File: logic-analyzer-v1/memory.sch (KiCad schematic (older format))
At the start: 8 parts

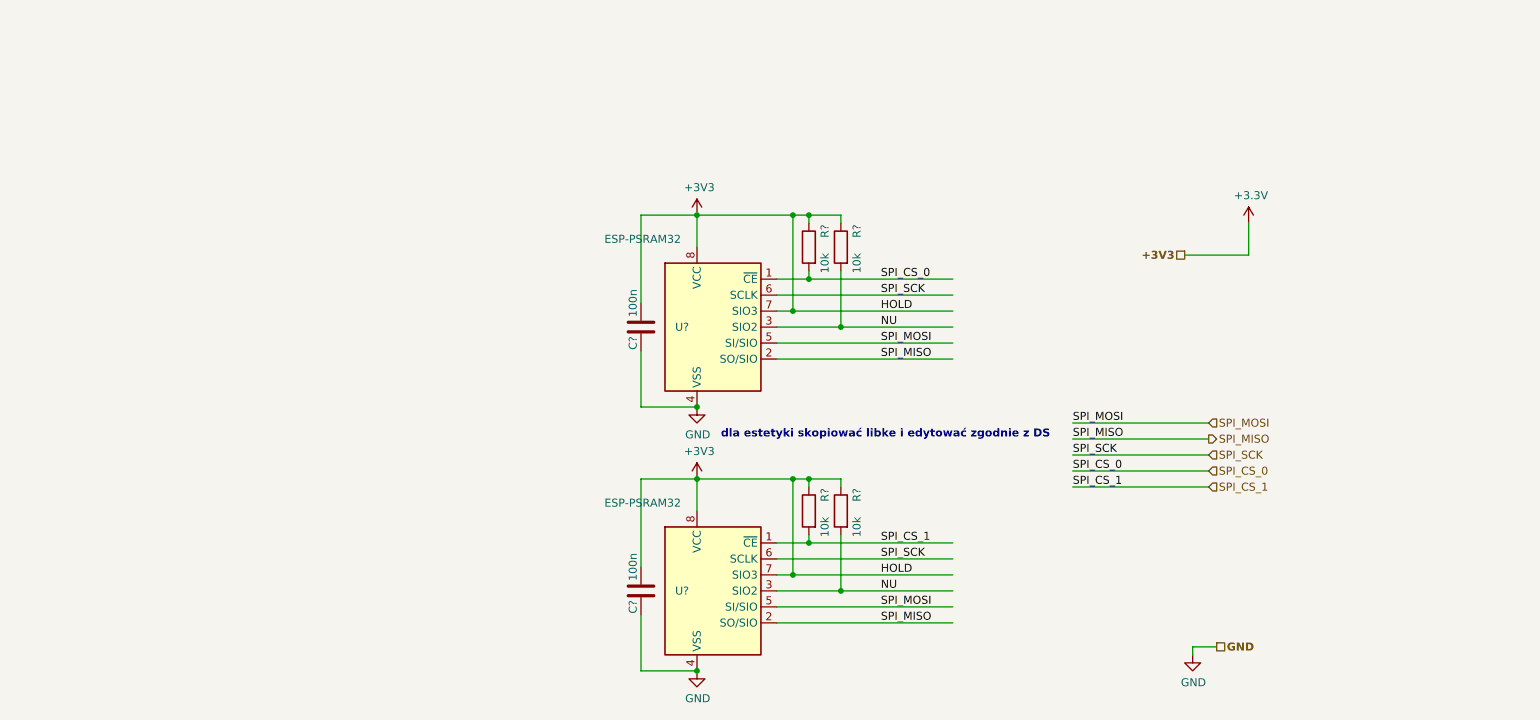
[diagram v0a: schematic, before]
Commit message: add comparator&sram
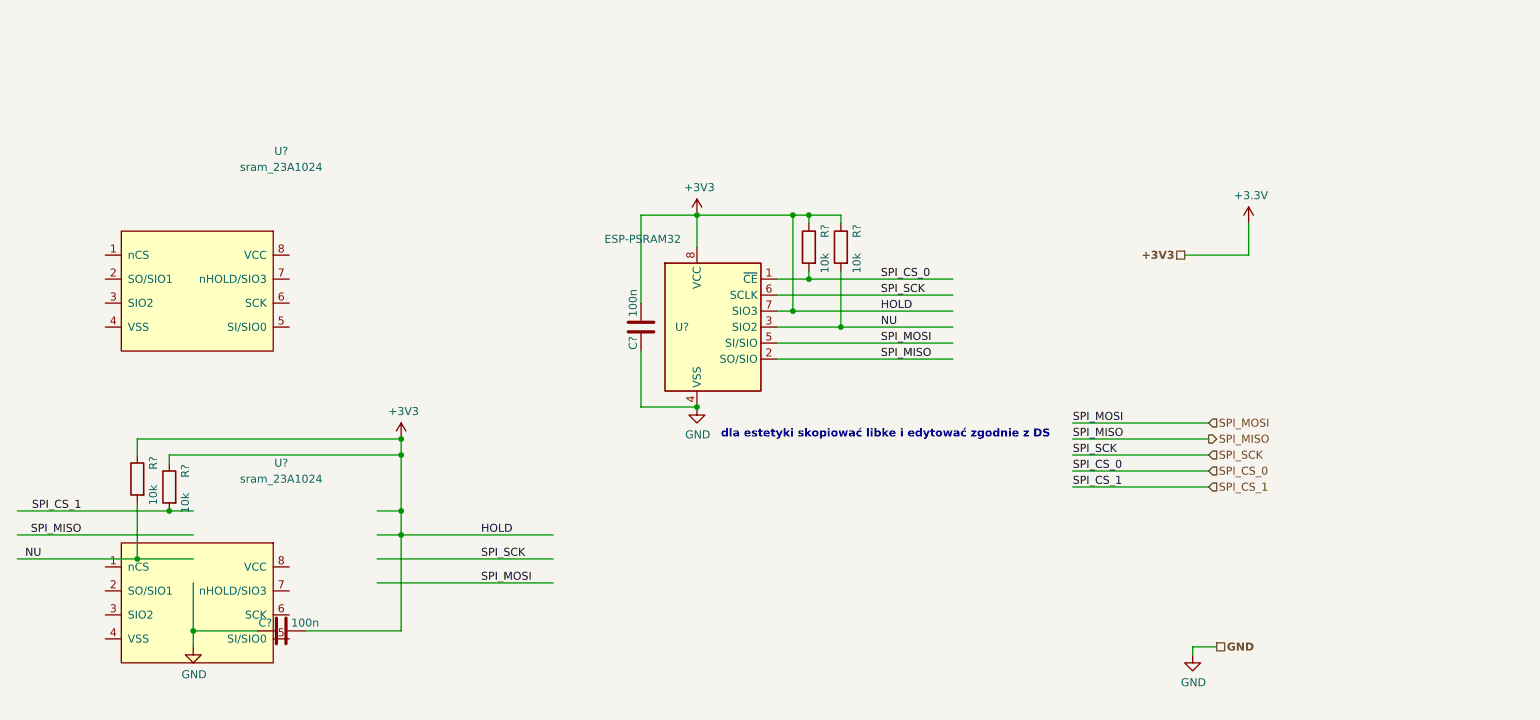
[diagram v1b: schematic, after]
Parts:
- removed C?: 100n, Capacitor_SMD:C_0603_1608Metric_Pad1.05x0.95mm_HandSolder, symbol Device:C
- removed U?: ESP-PSRAM32, Package_SO:SOIC-8_3.9x4.9mm_P1.27mm, symbol Memory_RAM:ESP-PSRAM32
- added C?: 100n, Capacitor_SMD:C_0603_1608Metric_Pad1.05x0.95mm_HandSolder, symbol Device:C
- added U? (x2): sram_23A1024, symbol New_Library:sram_23A1024
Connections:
- wire segments 53 -> 54
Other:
- moved on the sheet: R?
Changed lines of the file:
@@
 F 1 "ESP-PSRAM32" H 4800 3700 50  0000 R CNN
 F 2 "Package_SO:SOIC-8_3.9x4.9mm_P1.27mm" H 5000 2550 50  0001 C CNN
-F 3 "https://www.espressif.com/sites/default/files/documentation/esp-psram32_datasheet_en.pdf" H 4600 3650 50  0001 C CNN
+F 3 "https://www.tme.eu/Document/745fc52173836ec906dd19c8a3a18eb9/20005142C.pdf" H 4600 3650 50  0001 C CNN
 	1    5000 3150
 	1    0    0    -1
@@
 	4900 2450 4550 2450
 Connection ~ 4900 3650
-$Comp
-L Memory_RAM:ESP-PSRAM32 U?
-U 1 1 5FDC3CEF
-P 5000 4800
-AR Path="/5F19654C/5FDC3CEF" Ref="U?"  Part="1"
-AR Path="/5FDBE2FD/5FDC3CEF" Ref="U?"  Part="1"
-F 0 "U?" H 4850 4800 50  0000 R CNN
-F 1 "ESP-PSRAM32" H 4800 5350 50  0000 R CNN
-F 2 "Package_SO:SOIC-8_3.9x4.9mm_P1.27mm" H 5000 4200 50  0001 C CNN
-F 3 "https://www.espressif.com/sites/default/files/documentation/esp-psram32_datasheet_en.pdf" H 4600 5300 50  0001 C CNN
-	1    5000 4800
-	1    0    0    -1
-$EndComp
-$Comp
-L power:+3V3 #PWR?
-U 1 1 5FDC3CF5
-P 4900 4100
-AR Path="/5F19654C/5FDC3CF5" Ref="#PWR?"  Part="1"
-AR Path="/5FDBE2FD/5FDC3CF5" Ref="#PWR?"  Part="1"
-F 0 "#PWR?" H 4900 3950 50  0001 C CNN
-F 1 "+3V3" H 4915 4273 50  0000 C CNN
-F 2 "" H 4900 4100 50  0001 C CNN
-F 3 "" H 4900 4100 50  0001 C CNN
-	1    4900 4100
-	1    0    0    -1
-$EndComp
-$Comp
-L power:GND #PWR?
-U 1 1 5FDC3CFB
-P 4900 5300
-AR Path="/5F19654C/5FDC3CFB" Ref="#PWR?"  Part="1"
-AR Path="/5FDBE2FD/5FDC3CFB" Ref="#PWR?"  Part="1"
-F 0 "#PWR?" H 4900 5050 50  0001 C CNN
-F 1 "GND" H 4905 5127 50  0000 C CNN
-F 2 "" H 4900 5300 50  0001 C CNN
-F 3 "" H 4900 5300 50  0001 C CNN
-	1    4900 5300
-	1    0    0    -1
-$EndComp
-$Comp
-L Device:C C?
-U 1 1 5FDC3D17
-P 4550 4800
-AR Path="/5F19654C/5FDC3D17" Ref="C?"  Part="1"
-AR Path="/5FDBE2FD/5FDC3D17" Ref="C?"  Part="1"
-F 0 "C?" V 4500 4700 50  0000 C CNN
-F 1 "100n" V 4500 4950 50  0000 C CNN
-F 2 "Capacitor_SMD:C_0603_1608Metric_Pad1.05x0.95mm_HandSolder" H 4588 4650 50  0001 C CNN
-F 3 "~" H 4550 4800 50  0001 C CNN
-	1    4550 4800
-	1    0    0    -1
-$EndComp
-Wire Wire Line
-	4900 5300 4550 5300
-Wire Wire Line
-	4550 5300 4550 4950
-Wire Wire Line
-	4900 4100 4550 4100
-Connection ~ 4900 5300
 Text Notes 5050 3850 0    50   ~ 10
 dla estetyki skopiować libke i edytować zgodnie z DS
@@
 Wire Wire Line
 	5600 2850 6500 2850
-Text Label 6050 4900 0    50   ~ 0
-SPI_MOSI
-Text Label 6050 5000 0    50   ~ 0
+Text Label 1050 4450 2    50   ~ 0
 SPI_MISO
-Text Label 6050 4600 0    50   ~ 0
+Text Label 3550 4600 0    50   ~ 0
 SPI_SCK
-Text Label 6050 4500 0    50   ~ 0
+Text Label 1050 4300 2    50   ~ 0
 SPI_CS_1
-Text Label 6050 4700 0    50   ~ 0
-HOLD
 $Comp
 L Device:R R?
 U 1 1 5FDDAAEC
-P 5800 4300
+P 1400 4100
 AR Path="/5F08ED8D/5FDDAAEC" Ref="R?"  Part="1"
 AR Path="/5F19654C/5FDDAAEC" Ref="R?"  Part="1"
 AR Path="/5FDBE2FD/5FDDAAEC" Ref="R?"  Part="1"
-F 0 "R?" V 5700 4400 50  0000 C CNN
-F 1 "10k" V 5700 4200 50  0000 C CNN
-F 2 "Resistor_SMD:R_0603_1608Metric_Pad1.05x0.95mm_HandSolder" V 5730 4300 50  0001 C CNN
-F 3 "~" H 5800 4300 50  0001 C CNN
-	1    5800 4300
+F 0 "R?" V 1300 4200 50  0000 C CNN
+F 1 "10k" V 1300 4000 50  0000 C CNN
+F 2 "Resistor_SMD:R_0603_1608Metric_Pad1.05x0.95mm_HandSolder" V 1330 4100 50  0001 C CNN
+F 3 "~" H 1400 4100 50  0001 C CNN
+	1    1400 4100
 	-1   0    0    -1
 $EndComp
@@
 L Device:R R?
 U 1 1 5FDDAAF2
-P 5600 4300
+P 1600 4150
 AR Path="/5F08ED8D/5FDDAAF2" Ref="R?"  Part="1"
 AR Path="/5F19654C/5FDDAAF2" Ref="R?"  Part="1"
 AR Path="/5FDBE2FD/5FDDAAF2" Ref="R?"  Part="1"
-F 0 "R?" V 5500 4400 50  0000 C CNN
-F 1 "10k" V 5500 4200 50  0000 C CNN
-F 2 "Resistor_SMD:R_0603_1608Metric_Pad1.05x0.95mm_HandSolder" V 5530 4300 50  0001 C CNN
-F 3 "~" H 5600 4300 50  0001 C CNN
-	1    5600 4300
+F 0 "R?" V 1500 4250 50  0000 C CNN
+F 1 "10k" V 1500 4050 50  0000 C CNN
+F 2 "Resistor_SMD:R_0603_1608Metric_Pad1.05x0.95mm_HandSolder" V 1530 4150 50  0001 C CNN
+F 3 "~" H 1600 4150 50  0001 C CNN
+	1    1600 4150
 	-1   0    0    -1
 $EndComp
-Text Label 6050 4800 0    50   ~ 0
+Text Label 800  4600 2    50   ~ 0
 NU
 Wire Wire Line
-	5600 4150 5600 4100
-Connection ~ 5600 4100
-Wire Wire Line
-	5600 4100 5800 4100
-Wire Wire Line
-	5800 4100 5800 4150
-Wire Wire Line
-	4900 4100 5500 4100
-Wire Wire Line
-	5500 4700 5500 4100
-Connection ~ 5500 4100
-Wire Wire Line
-	5500 4100 5600 4100
-Wire Wire Line
-	5500 4700 5400 4700
-Connection ~ 5500 4700
-Wire Wire Line
-	5400 4900 6500 4900
-Wire Wire Line
-	5400 5000 6500 5000
-Wire Wire Line
-	5400 4800 5800 4800
-Wire Wire Line
-	5500 4700 6500 4700
-Wire Wire Line
-	5400 4600 6500 4600
-Wire Wire Line
-	5400 4500 5600 4500
-Wire Wire Line
-	5800 4450 5800 4800
-Connection ~ 5800 4800
-Wire Wire Line
-	5800 4800 6500 4800
-Wire Wire Line
-	5600 4450 5600 4500
-Connection ~ 5600 4500
-Wire Wire Line
-	5600 4500 6500 4500
-Connection ~ 4900 4100
-Wire Wire Line
-	4550 4100 4550 4650
-Wire Wire Line
-	4900 4300 4900 4100
+	1750 4450 650  4450
+Wire Wire Line
+	2900 4600 4000 4600
+Wire Wire Line
+	1750 4600 1400 4600
+Wire Wire Line
+	1750 4300 1600 4300
 Text HLabel 8100 3750 2    50   Input ~ 0
 SPI_MOSI
@@
 Wire Wire Line
 	8350 2700 8350 2500
+$Comp
+L New_Library:sram_23A1024 U?
+U 1 1 6063BECA
+P 1750 2900
+F 0 "U?" H 2300 3750 50  0000 C CNN
+F 1 "sram_23A1024" H 2300 3650 50  0000 C CNN
+F 2 "" H 2300 3600 50  0001 C CNN
+F 3 "https://www.tme.eu/pl/details/23lc1024-i_sn/pamieci-sram-szeregowe/microchip-technology/" H 2300 3600 50  0001 C CNN
+	1    1750 2900
+	1    0    0    -1
+$EndComp
+$Comp
+L New_Library:sram_23A1024 U?
+U 1 1 6064CBA0
+P 1750 4850
+F 0 "U?" H 2300 5700 50  0000 C CNN
+F 1 "sram_23A1024" H 2300 5600 50  0000 C CNN
+F 2 "" H 2300 5550 50  0001 C CNN
+F 3 "https://www.tme.eu/pl/details/23lc1024-i_sn/pamieci-sram-szeregowe/microchip-technology/" H 2300 5550 50  0001 C CNN
+	1    1750 4850
+	1    0    0    -1
+$EndComp
+$Comp
+L Device:C C?
+U 1 1 6064CE71
+P 2300 5050
+AR Path="/5F19654C/6064CE71" Ref="C?"  Part="1"
+AR Path="/5FDBE2FD/6064CE71" Ref="C?"  Part="1"
+F 0 "C?" V 2250 4950 50  0000 C CNN
+F 1 "100n" V 2250 5200 50  0000 C CNN
+F 2 "Capacitor_SMD:C_0603_1608Metric_Pad1.05x0.95mm_HandSolder" H 2338 4900 50  0001 C CNN
+F 3 "~" H 2300 5050 50  0001 C CNN
+	1    2300 5050
+	0    1    1    0
+$EndComp
+Wire Wire Line
+	2900 4300 3050 4300
+Wire Wire Line
+	3050 4300 3050 4450
+Wire Wire Line
+	3050 5050 2450 5050
+Wire Wire Line
+	1750 4750 1750 5050
+Wire Wire Line
+	1750 5050 2150 5050
+Wire Wire Line
+	3050 4300 3050 3950
+Connection ~ 3050 4300
+$Comp
+L power:GND #PWR?
+U 1 1 6065064B
+P 1750 5150
+AR Path="/5F19654C/6065064B" Ref="#PWR?"  Part="1"
+AR Path="/5FDBE2FD/6065064B" Ref="#PWR?"  Part="1"
+F 0 "#PWR?" H 1750 4900 50  0001 C CNN
+F 1 "GND" H 1755 4977 50  0000 C CNN
+F 2 "" H 1750 5150 50  0001 C CNN
+F 3 "" H 1750 5150 50  0001 C CNN
+	1    1750 5150
+	1    0    0    -1
+$EndComp
+$Comp
+L power:+3V3 #PWR?
+U 1 1 60650961
+P 3050 3850
+AR Path="/5F19654C/60650961" Ref="#PWR?"  Part="1"
+AR Path="/5FDBE2FD/60650961" Ref="#PWR?"  Part="1"
+F 0 "#PWR?" H 3050 3700 50  0001 C CNN
+F 1 "+3V3" H 3065 4023 50  0000 C CNN
+F 2 "" H 3050 3850 50  0001 C CNN
+F 3 "" H 3050 3850 50  0001 C CNN
+	1    3050 3850
+	1    0    0    -1
+$EndComp
+Text Label 3550 4450 0    50   ~ 0
+HOLD
+Wire Wire Line
+	2900 4750 4000 4750
+Text Label 3550 4750 0    50   ~ 0
+SPI_MOSI
+Wire Wire Line
+	2900 4450 3050 4450
+Connection ~ 3050 4450
+Wire Wire Line
+	3050 4450 3050 5050
+Wire Wire Line
+	3050 4450 4000 4450
+Connection ~ 1600 4300
+Wire Wire Line
+	1600 4300 650  4300
+Wire Wire Line
+	1600 4000 1600 3950
+Wire Wire Line
+	1600 3950 3050 3950
+Connection ~ 3050 3950
+Wire Wire Line
+	3050 3950 3050 3850
+Wire Wire Line
+	3050 3850 1400 3850
+Connection ~ 3050 3850
+Wire Wire Line
+	1400 3850 1400 3950
+Wire Wire Line
+	1400 4250 1400 4600
+Connection ~ 1400 4600
+Wire Wire Line
+	1400 4600 650  4600
+Connection ~ 1750 5050
+Wire Wire Line
+	1750 5050 1750 5150
 $EndSCHEMATC

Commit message: MOD uart port direction, minor cosmetic changes
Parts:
- U? (x2): symbol New_Library:sram_23A1024 -> logic-analyzer-v1-rescue:sram_23A1024-New_Library
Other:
- moved on the sheet: U?
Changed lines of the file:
@@
 $Descr A4 11693 8268
 encoding utf-8
-Sheet 5 6
+Sheet 5 8
 Title ""
 Date ""
@@
 	8350 2700 8350 2500
 $Comp
-L New_Library:sram_23A1024 U?
+L logic-analyzer-v1-rescue:sram_23A1024-New_Library U?
 U 1 1 6063BECA
 P 1750 2900
@@
 $EndComp
 $Comp
-L New_Library:sram_23A1024 U?
+L logic-analyzer-v1-rescue:sram_23A1024-New_Library U?
 U 1 1 6064CBA0
 P 1750 4850

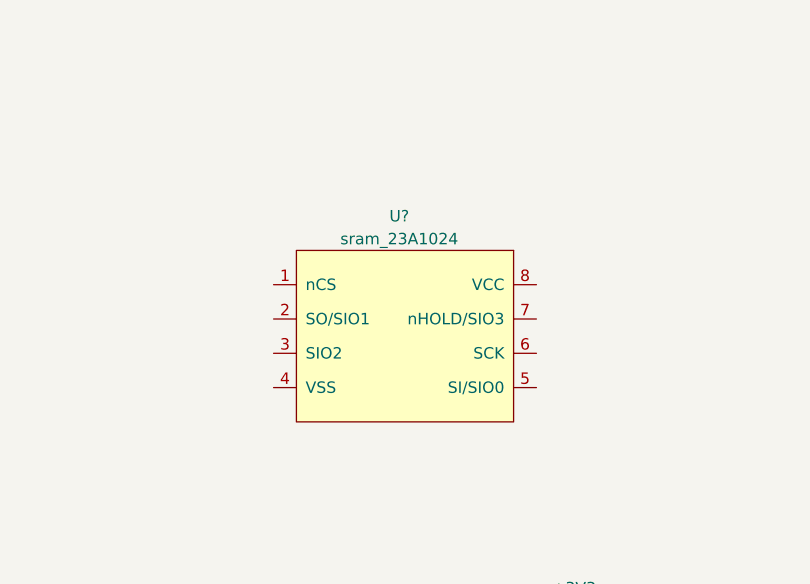
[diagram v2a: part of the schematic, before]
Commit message: improvement origin in libraries and creation my_library containing all ours libraries
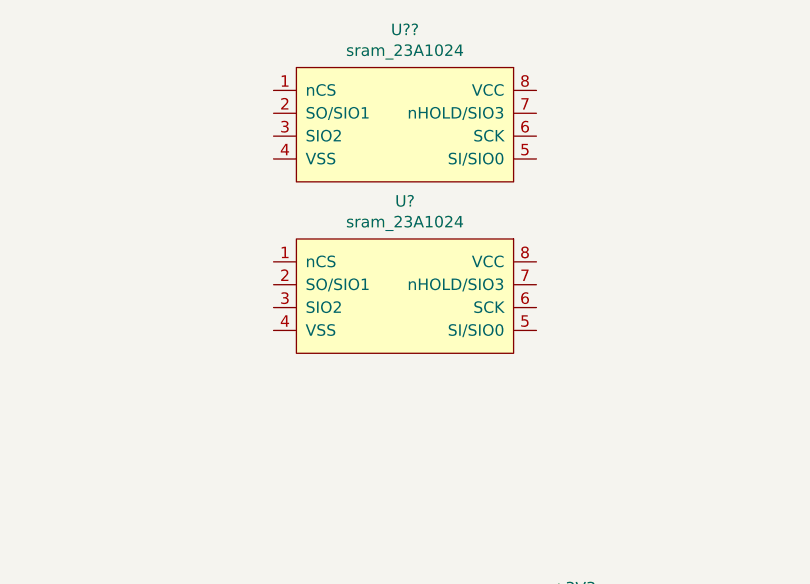
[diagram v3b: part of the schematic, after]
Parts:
- removed U?: sram_23A1024, symbol logic-analyzer-v1-rescue:sram_23A1024-New_Library
- added U?, U??: sram_23A1024, symbol my_library:sram_23A1024
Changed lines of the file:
@@
 $Descr A4 11693 8268
 encoding utf-8
-Sheet 5 8
+Sheet 7 8
 Title ""
 Date ""
@@
 $Comp
 L logic-analyzer-v1-rescue:sram_23A1024-New_Library U?
-U 1 1 6063BECA
-P 1750 2900
-F 0 "U?" H 2300 3750 50  0000 C CNN
-F 1 "sram_23A1024" H 2300 3650 50  0000 C CNN
-F 2 "" H 2300 3600 50  0001 C CNN
-F 3 "https://www.tme.eu/pl/details/23lc1024-i_sn/pamieci-sram-szeregowe/microchip-technology/" H 2300 3600 50  0001 C CNN
-	1    1750 2900
-	1    0    0    -1
-$EndComp
-$Comp
-L logic-analyzer-v1-rescue:sram_23A1024-New_Library U?
 U 1 1 6064CBA0
 P 1750 4850
@@
 Wire Wire Line
 	1750 5050 1750 5150
+$Comp
+L my_library:sram_23A1024 U??
+U 1 1 60877B38
+P 2300 1650
+F 0 "U??" H 2325 2065 50  0000 C CNN
+F 1 "sram_23A1024" H 2325 1974 50  0000 C CNN
+F 2 "" H 2300 2000 50  0001 C CNN
+F 3 "" H 2300 2000 50  0001 C CNN
+	1    2300 1650
+	1    0    0    -1
+$EndComp
+$Comp
+L my_library:sram_23A1024 U?
+U 1 1 60878112
+P 2300 2400
+F 0 "U?" H 2325 2815 50  0000 C CNN
+F 1 "sram_23A1024" H 2325 2724 50  0000 C CNN
+F 2 "" H 2300 2750 50  0001 C CNN
+F 3 "" H 2300 2750 50  0001 C CNN
+	1    2300 2400
+	1    0    0    -1
+$EndComp
 $EndSCHEMATC

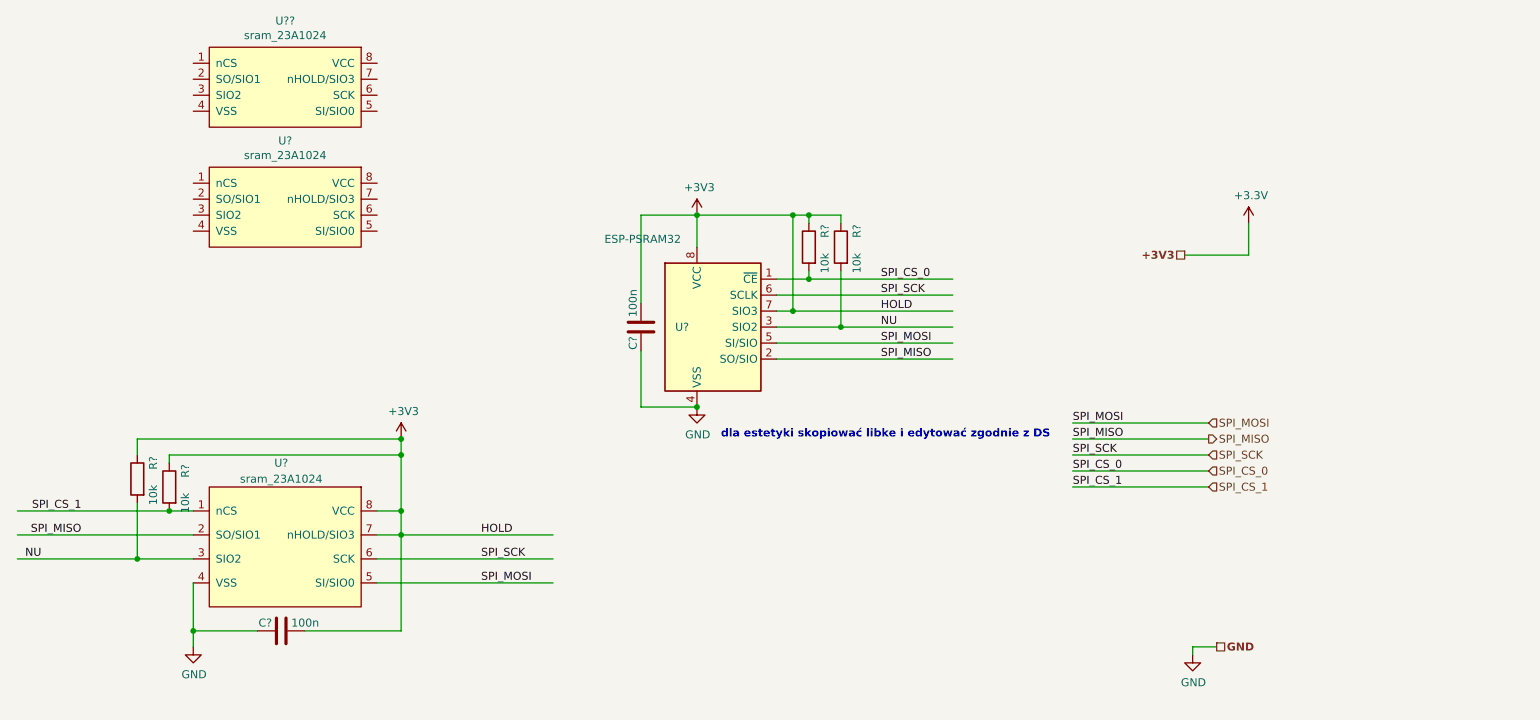
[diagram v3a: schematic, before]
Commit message: changing sram blocks from new library
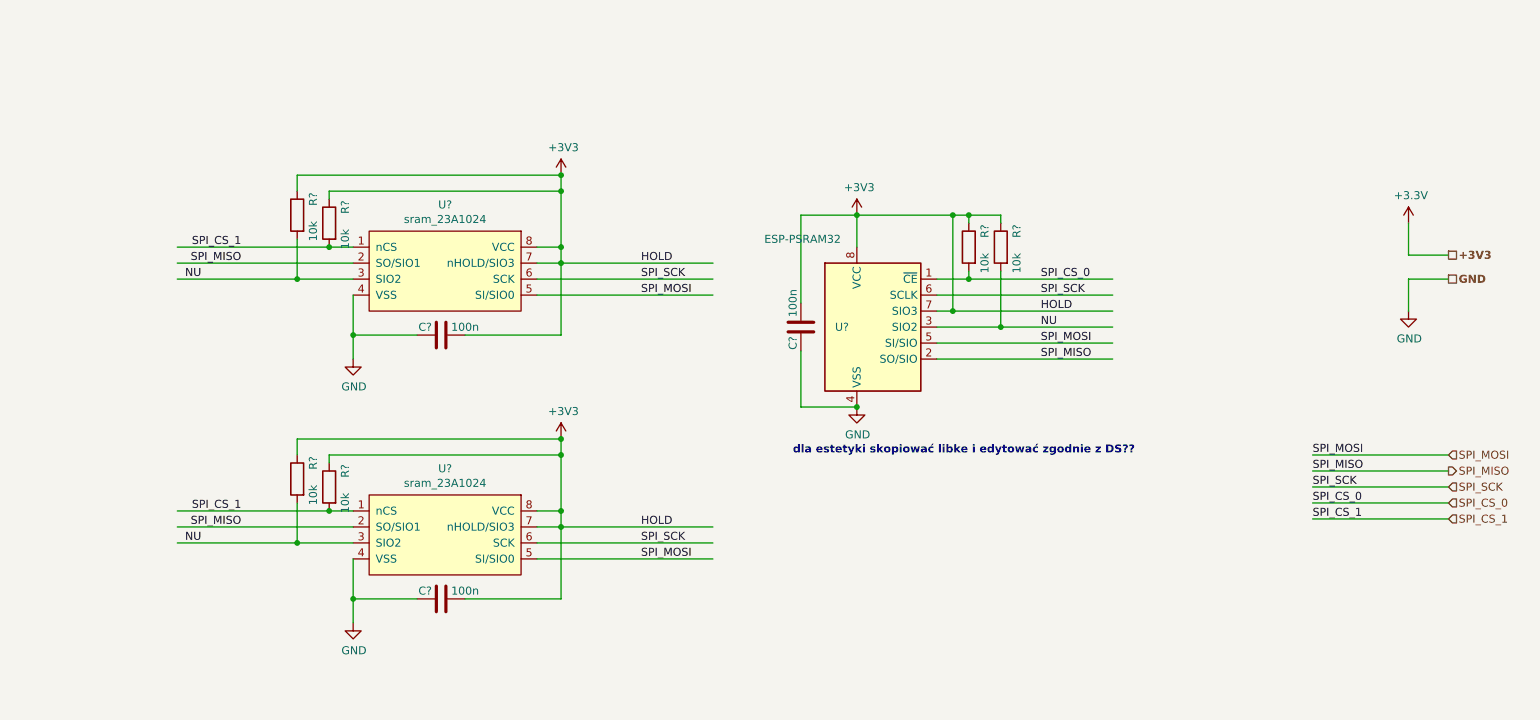
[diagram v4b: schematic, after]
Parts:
- removed U?: sram_23A1024, symbol logic-analyzer-v1-rescue:sram_23A1024-New_Library
- removed U??: sram_23A1024, symbol my_library:sram_23A1024
- added C?: 100n, Capacitor_SMD:C_0603_1608Metric_Pad1.05x0.95mm_HandSolder, symbol Device:C
- added R? (x2): 10k, Resistor_SMD:R_0603_1608Metric_Pad1.05x0.95mm_HandSolder, symbol Device:R
- added U?: sram_23A1024, symbol my_library:sram_23A1024
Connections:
- wire segments 54 -> 77
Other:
- note added: "dla estetyki skopiować libke i edytować zgodnie z DS??"
- note removed: "dla estetyki skopiować libke i edytować zgodnie z DS"
- moved on the sheet: C?, R?, U?
